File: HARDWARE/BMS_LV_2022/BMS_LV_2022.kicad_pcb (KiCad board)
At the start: 2 copper layers, 90 x 45 mm, 169 parts, among them J1 Conn_01x06_Male, J10 Conn_01x01_Female, J2 Conn_01x12_Male, J3 USB_B_Mini, J4 Conn_01x01_Female, J5 Conn_01x01_Female, J6 Conn_01x01_Female, J7 Conn_01x01_Female, J8 Conn_01x01_Female, J9 Conn_01x01_Female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

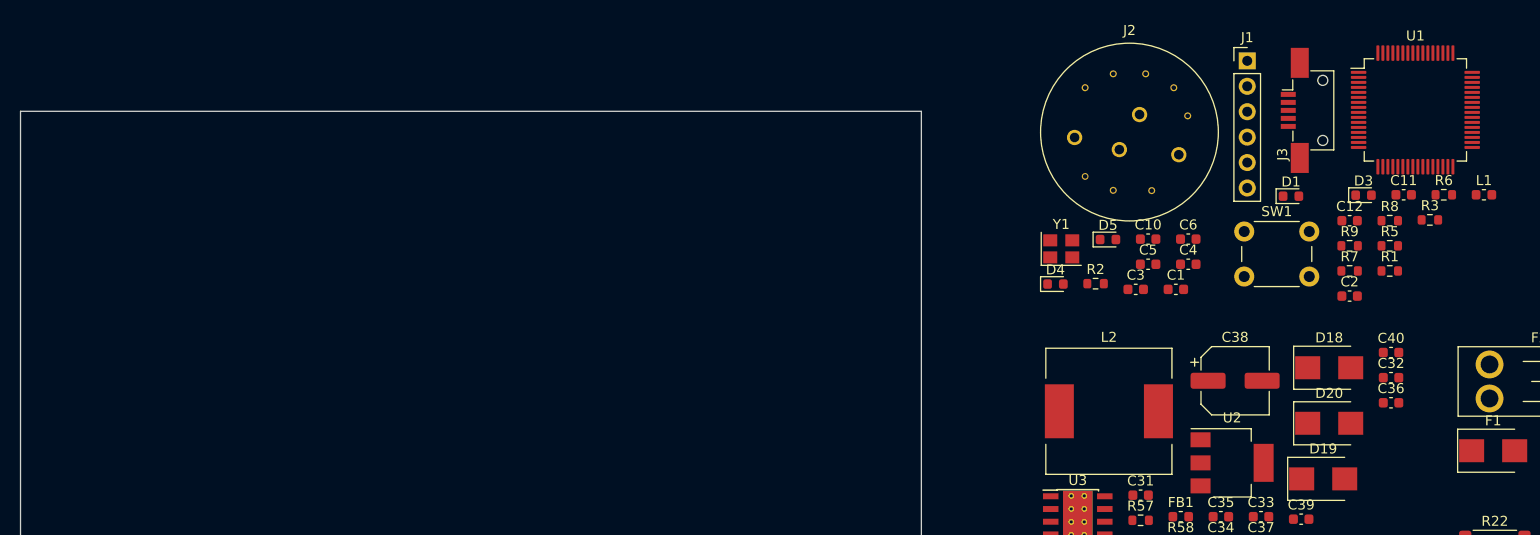
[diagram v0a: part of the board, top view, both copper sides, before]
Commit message: Thermistors change
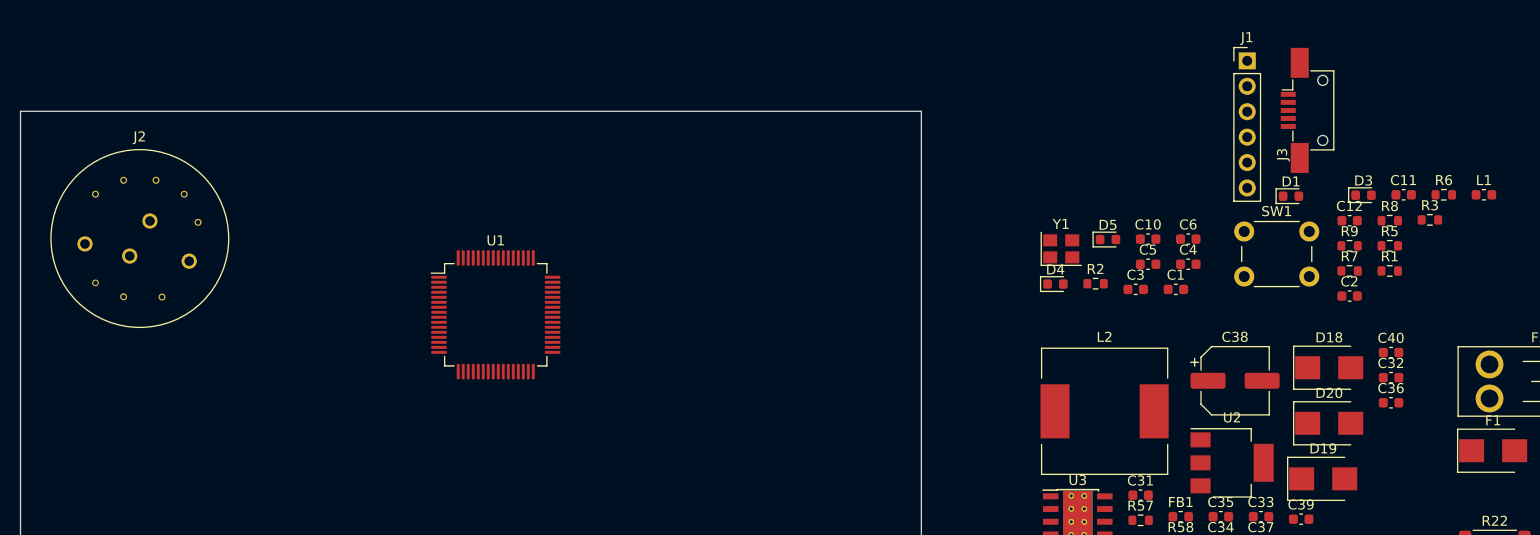
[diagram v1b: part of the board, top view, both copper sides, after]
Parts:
- moved J2 99.4 mm to (121.9, 92.7)
- moved U1 94.1 mm to (157.5, 100.3)
- moved L2 0.43 mm to (218.3, 110.0)

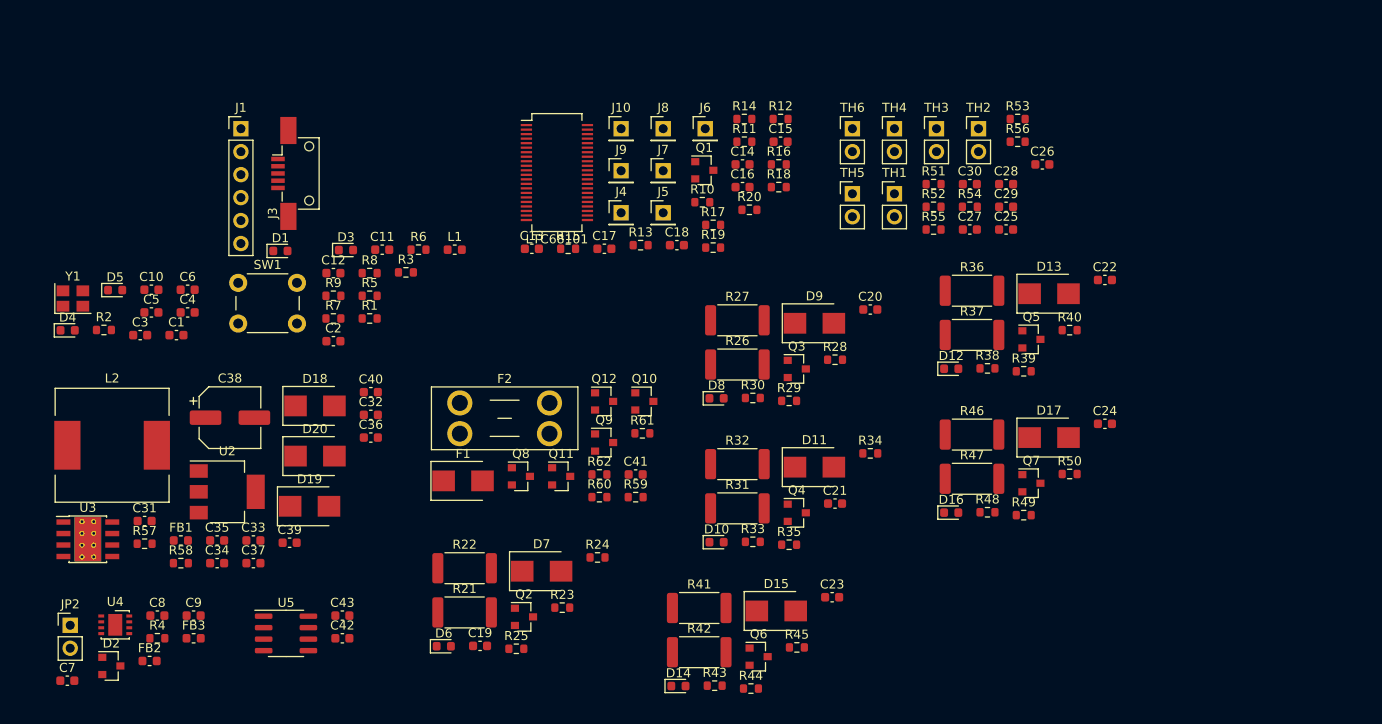
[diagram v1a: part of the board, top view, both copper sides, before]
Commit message: PCB update
Parts changed due to smaller footprints
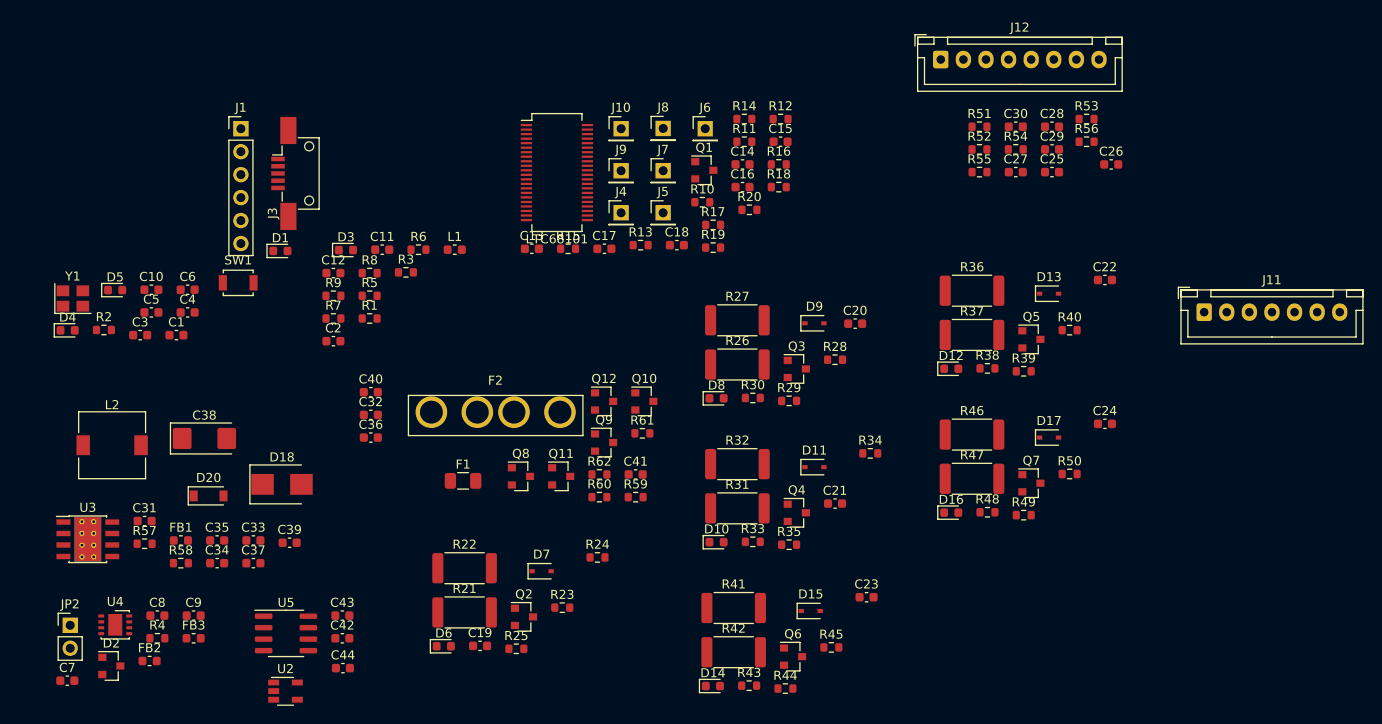
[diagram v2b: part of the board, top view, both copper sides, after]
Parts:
- removed D19: D_Schottky, Diode_SMD:D_SMB
- removed TH1, TH2, TH3, TH4, TH5, TH6: Thermistor_PTC, Connector_PinHeader_2.54mm:PinHeader_1x02_P2.54mm_Vertical
- added C44: 100nF, Capacitor_SMD:C_0603_1608Metric, F.Cu at (243.8, 134.6)
- added J11: Conn_01x07_Female, Connector_JST:JST_XH_B7B-XH-A_1x07_P2.50mm_Vertical, F.Cu at (339.1, 95.2)
- added J12: Conn_01x08_Female, Connector_JST:JST_XH_B8B-XH-A_1x08_P2.50mm_Vertical, F.Cu at (310.0, 67.3)
- C34, C36: value 100nF -> 1uF
- C38: footprint Capacitor_SMD:CP_Elec_6.3x7.7 -> Capacitor_Tantalum_SMD:CP_EIA-6032-28_Kemet-C
- D11, D13, D15, D17, D7, D9: footprint Diode_SMD:D_SMB -> Diode_SMD:D_SOD-323
- D20: footprint Diode_SMD:D_SMB -> Diode_SMD:D_SOD-123
- F1: footprint Diode_SMD:D_SMB -> Fuse:Fuse_1206_3216Metric
- F2: footprint Fuse:Fuseholder_Blade_Mini_Keystone_3568 -> footprints:Fuseholder_Keystone_3522-2
- L2: footprint Inductor_SMD:L_12x12mm_H8mm -> Inductor_SMD:L_7.3x7.3_H4.5
- R4: value 120R -> 120
- SW1: footprint Button_Switch_THT:SW_PUSH_6mm -> Button_Switch_SMD:SW_SPST_B3U-1000P
- U2: value LM1117-3.3 -> LD3985M33R_TSOT23; footprint Package_TO_SOT_SMD:SOT-223-3_TabPin2 -> Package_TO_SOT_SMD:TSOT-23-5
- moved U2 23.0 mm to (237.5, 137.2)
- moved D20 12.6 mm to (229.0, 115.6)
- moved D18 9.41 mm to (237.1, 114.3)
- moved C28 8.13 mm to (322.3, 74.7)
- moved C30 8.13 mm to (318.3, 74.7)
- moved R51 8.13 mm to (314.2, 74.7)
- moved C25 8.13 mm to (322.3, 79.8)
- moved C27 8.13 mm to (318.3, 79.8)
- moved C29 8.13 mm to (322.3, 77.2)
- moved R52 8.13 mm to (314.2, 77.2)
- moved R54 8.13 mm to (318.3, 77.2)
- moved R55 8.13 mm to (314.2, 79.8)
- moved C26 7.62 mm to (328.8, 78.9)
- moved R53 7.62 mm to (326.1, 73.9)
- moved R56 7.62 mm to (326.1, 76.4)
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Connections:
- net /LTC6810/Balance1/Cell renamed /LTC6810/CellBalance2
- net /LTC6810/Balance2/Cell renamed /LTC6810/CellBalance3
- net /LTC6810/Balance3/Cell renamed /LTC6810/CellBalance4
- net /LTC6810/Balance4/Cell renamed /LTC6810/CellBalance5
- net /LTC6810/Balance5/Cell renamed /LTC6810/CellBalance6
- J2 pad 10: Net-(J2-Pad10) -> /V_Out
- J2 pad 11: /V_Out -> GND
- J2 pad 9: Net-(J2-Pad9) -> /V_Out
- U2 pad 1: GND -> +5VD
- U2 pad 2: +3V3 -> GND
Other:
- copper layers 2 -> 4

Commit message: PCB Layout Update
Some work on PCB Layout
+ AS214-97PN (connector) 3D model added
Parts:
- removed J10, J4, J5, J6, J7, J8, J9: Conn_01x01_Female, Connector_PinHeader_2.54mm:PinHeader_1x01_P2.54mm_Vertical
- moved C24 217.1 mm to (111.7, 89.5), turned to 270 degrees
- moved R50 212.3 mm to (113.2, 89.5), turned to 270 degrees
- moved D17 207.9 mm to (114.9, 89.6), turned to 270 degrees
- moved R49 204.5 mm to (116.6, 89.5), turned to 270 degrees
- moved Q7 202.4 mm to (119.0, 89.8)
- moved R46 201.5 mm to (113.5, 84.2), turned to 90 degrees
- moved R48 198.3 mm to (120.0, 81.9), turned to 90 degrees
- moved R47 198.3 mm to (117.3, 84.2), turned to 90 degrees
- moved D16 193.6 mm to (120.0, 86.5), turned to 90 degrees
- moved C22 184.4 mm to (143.7, 93.7), turned to 180 degrees
- moved D13 182.2 mm to (139.8, 89.6), turned to 270 degrees
- moved R40 180.6 mm to (143.7, 92.2), turned to 180 degrees
- moved R39 178.1 mm to (141.5, 89.5), turned to 270 degrees
- moved Q5 176.3 mm to (143.9, 89.8)
- moved R36 175.3 mm to (138.4, 84.2), turned to 90 degrees
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
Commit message: PCB Layout Update 2
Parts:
- moved C9 98.4 mm to (132.1, 103.8), turned to 90 degrees
- moved FB3 97.2 mm to (134.9, 101.4)
- moved D1 95.2 mm to (178.4, 120.2), turned to 270 degrees
- moved FB2 94.3 mm to (132.1, 106.7), turned to 270 degrees
- moved SW1 94.1 mm to (145.7, 113.1), turned to 180 degrees
- moved R4 93.7 mm to (132.1, 109.7), turned to 90 degrees
- moved D3 93.5 mm to (179.9, 120.2), turned to 270 degrees
- moved D2 93.1 mm to (132.6, 97.6), turned to 195 degrees
- moved R2 93.1 mm to (178.4, 123.2), turned to 270 degrees
- moved D4 91.8 mm to (181.4, 120.2), turned to 270 degrees
- moved C8 91.7 mm to (134.9, 104.4)
- moved R3 91.3 mm to (179.9, 123.2), turned to 270 degrees
- moved C1 90.6 mm to (148.9, 113.3), turned to 90 degrees
- moved D5 90.1 mm to (182.8, 120.2), turned to 270 degrees
- moved R5 89.5 mm to (181.4, 123.2), turned to 270 degrees
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
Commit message: PCB Layout Update 3
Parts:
- removed R13, R14, R15: 10k, Resistor_SMD:R_0603_1608Metric
- added J4: Battery+, footprints:CellPad, F.Cu at (114.1, 91.7)
- added J5: Battery-, footprints:CellPad, F.Cu at (114.1, 115.3)
- Q11, Q12, Q8, Q9: value Q_PMOS_GSD -> SiSS05DN; footprint Package_TO_SOT_SMD:SOT-23 -> Package_SO:Vishay_PowerPAK_1212-8_Single
- moved Q9 117.2 mm to (116.4, 85.9), turned to 180 degrees
- moved Q10 116.1 mm to (129.1, 82.1)
- moved R61 116.1 mm to (126.7, 82.0)
- moved R59 116.1 mm to (132.3, 83.1), turned to 0 degrees
- moved R60 116.0 mm to (132.3, 81.7), turned to 0 degrees
- moved Q12 114.4 mm to (120.8, 82.3), turned to 0 degrees
- moved Q8 114.3 mm to (116.4, 82.3), turned to 180 degrees
- moved C41 114.2 mm to (124.4, 82.7)
- moved R62 114.0 mm to (124.4, 81.2)
- moved Q11 110.3 mm to (120.7, 85.9), turned to 0 degrees
- moved F1 108.8 mm to (120.6, 92.6), turned to 90 degrees
- moved F2 96.7 mm to (132.8, 86.2), turned to 180 degrees
- moved C42 84.1 mm to (141.6, 93.0)
- moved U5 84.1 mm to (137.2, 91.6)
- moved C43 83.0 mm to (142.4, 89.7), turned to 0 degrees
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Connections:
- C13 pad 2: GND -> GNDPWR
- C14 pad 2: GND -> GNDPWR
- C15 pad 2: GND -> GNDPWR
- C16 pad 2: GND -> GNDPWR
- C17 pad 2: GND -> GNDPWR
- C18 pad 1: GND -> GNDPWR
- C19 pad 2: GND -> GNDPWR
- C20 pad 2: GND -> GNDPWR
- C21 pad 2: GND -> GNDPWR
- C22 pad 2: GND -> GNDPWR
- C23 pad 2: GND -> GNDPWR
- C24 pad 2: GND -> GNDPWR
- D17 pad 2: GND -> GNDPWR
- J11 pad 1: +24V -> +BATT
- J11 pad 7: GND -> GNDPWR
- J2 pad 6: Net-(J2-Pad6) -> VCC
- J2 pad 8: VCC -> Net-(J2-Pad8)
- LTC68101 pad 1: GND -> GNDPWR
- LTC68101 pad 21: GND -> GNDPWR
- LTC68101 pad 22: GND -> GNDPWR
- LTC68101 pad 23: GND -> GNDPWR
- LTC68101 pad 24: GND -> GNDPWR
- LTC68101 pad 28: GND -> GNDPWR
- LTC68101 pad 29: GND -> GNDPWR
- LTC68101 pad 35: Net-(LTC68101-Pad35) -> Net-(LTC68101-Pad34)
- LTC68101 pad 38: Net-(LTC68101-Pad38) -> Net-(LTC68101-Pad34)
- LTC68101 pad 39: Net-(LTC68101-Pad39) -> Net-(LTC68101-Pad34)
- LTC68101 pad 43: GND -> GNDPWR
- LTC68101 pad 44: GND -> GNDPWR
- Q11 pad 1: /eFuse/Gate -> Net-(C41-Pad2)
- Q11 pad 3: Net-(F2-Pad2) -> Net-(C41-Pad2)
- Q12 pad 1: /eFuse/Gate -> Net-(C41-Pad2)
- Q12 pad 3: Net-(F2-Pad2) -> Net-(C41-Pad2)
- Q7 pad 2: GND -> GNDPWR
- Q8 pad 1: /eFuse/Gate -> Net-(C41-Pad2)
- Q8 pad 3: +24V -> Net-(C41-Pad2)
- Q9 pad 1: /eFuse/Gate -> Net-(C41-Pad2)
- Q9 pad 3: +24V -> Net-(C41-Pad2)
- R10 pad 2: +24V -> +BATT
- R11 pad 2: +24V -> +BATT
- R12 pad 1: GND -> GNDPWR
- R12 pad 2: Net-(LTC68101-Pad39) -> Net-(LTC68101-Pad34)
- R19 pad 2: +24V -> +BATT
- R21 pad 2: +24V -> +BATT
- R22 pad 2: +24V -> +BATT
- R23 pad 2: +24V -> +BATT
- R49 pad 2: GND -> GNDPWR
- R50 pad 2: GND -> GNDPWR
- Y1 pad 1: Net-(C5-Pad2) -> Net-(C6-Pad2)
- Y1 pad 2: Net-(C6-Pad2) -> GND
- Y1 pad 3: (no net) -> Net-(C5-Pad2)
- Y1 pad 4: (no net) -> GND
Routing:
- net /LTC6810/CellBalance5: track 0.00 -> 34.6 mm
- net /LTC6810/CellBalance3: track 0.00 -> 34.0 mm
- net /LTC6810/CellBalance4: track 0.00 -> 25.0 mm
- net /LTC6810/CellBalance2: track 0.00 -> 23.2 mm
- net /LTC6810/CellBalance6: track 0.00 -> 20.5 mm
- net +BATT: track 0.00 -> 16.0 mm
- net GNDPWR: track 0.00 -> 11.8 mm
- net /VCC_Pin: track 0.00 -> 3.43 mm
- net (no net): vias 0 -> 4

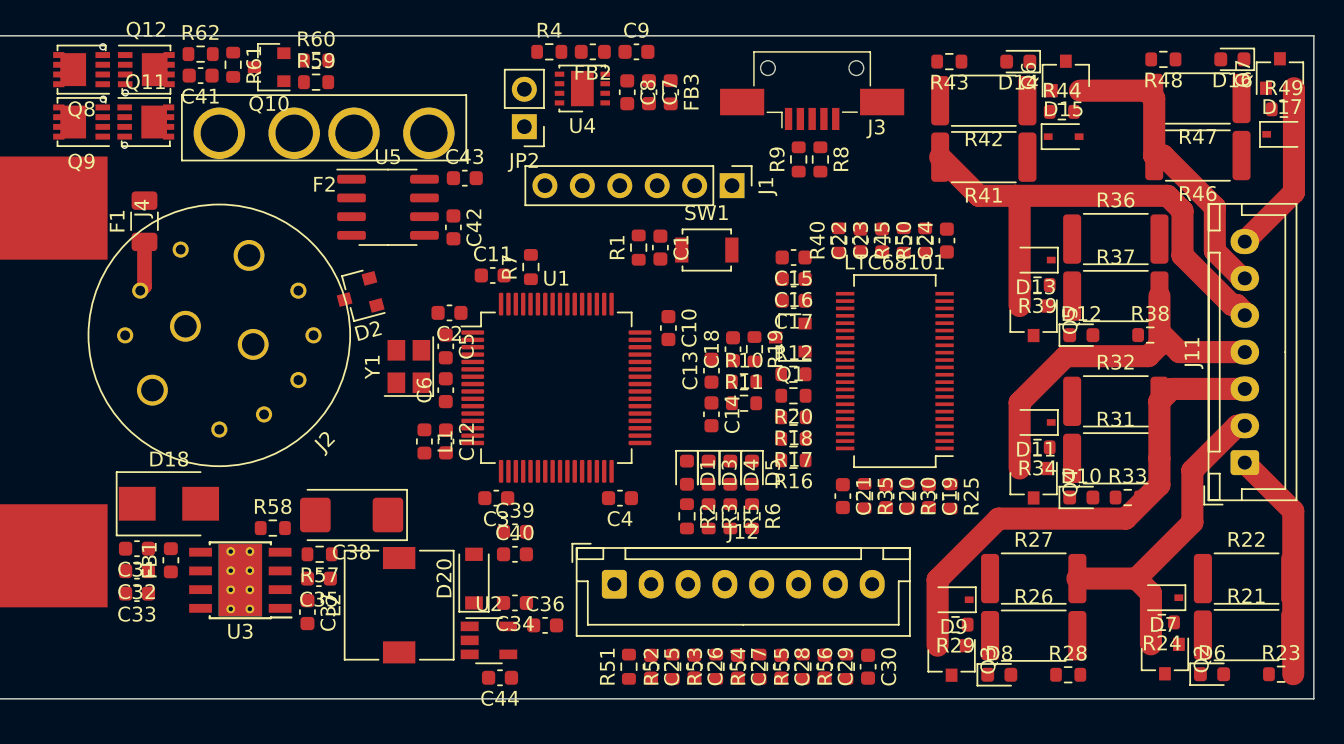
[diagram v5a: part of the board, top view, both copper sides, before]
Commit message: Power planes added
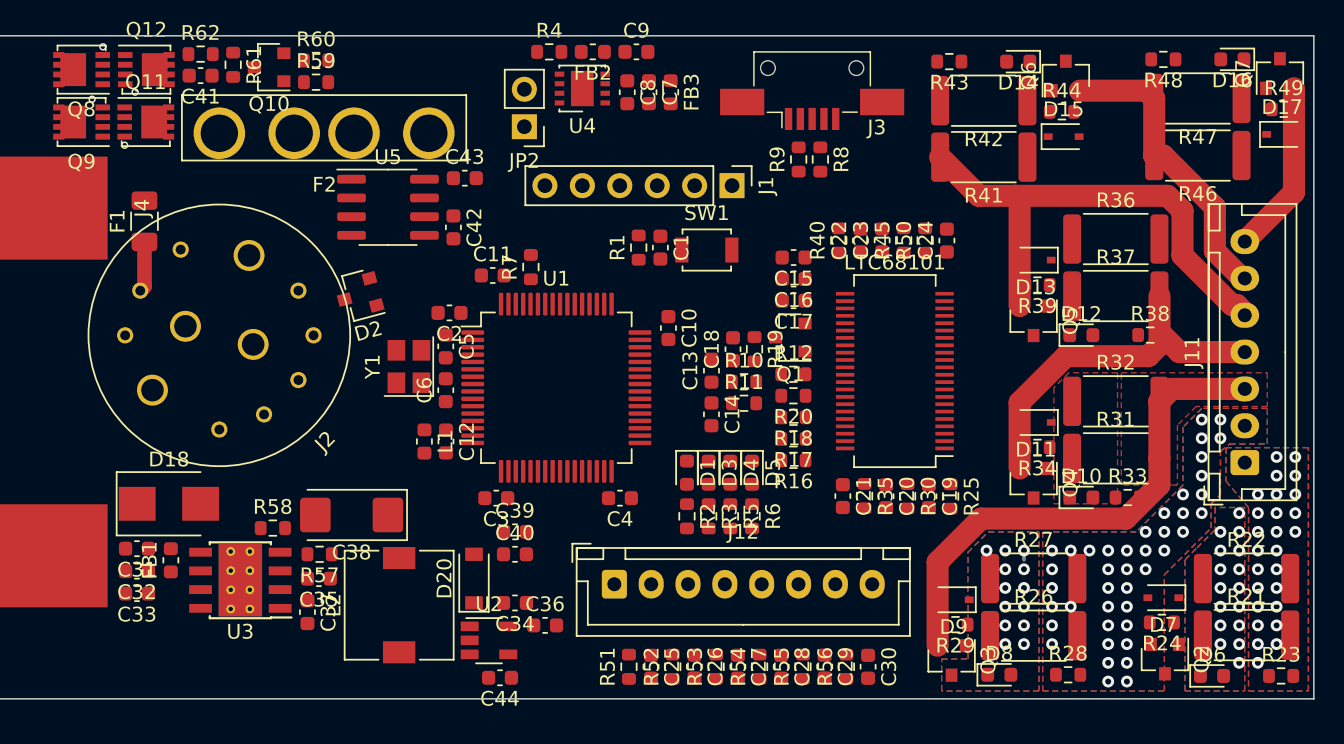
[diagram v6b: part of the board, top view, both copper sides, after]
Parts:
- moved D6 0.11 mm to (193.1, 123.4)
- moved R23 0.11 mm to (197.8, 123.4)
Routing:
- net /LTC6810/CellBalance2: track 23.2 -> 0.64 mm, vias 0 -> 42
- net +BATT: track 16.0 -> 0.29 mm, vias 0 -> 26
- net /LTC6810/CellBalance3: track 34.0 -> 34.7 mm
- net Net-(D8-Pad1): track 0.00 -> 0.63 mm, vias 0 -> 13
- net Net-(D6-Pad1): vias 0 -> 16
- added copper zone on B.Cu, net +BATT
- added copper zone on F.Cu, net +BATT
- added copper zone on B.Cu, net /LTC6810/CellBalance2
- added copper zone on F.Cu, net /LTC6810/CellBalance2
- added copper zone on F.Cu, net /LTC6810/CellBalance3
- added copper zone on In2.Cu, net GND
- added copper zone on In2.Cu, net GNDPWR
- added copper zone on F.Cu, net Net-(D10-Pad1)
- added copper zone on B.Cu, net Net-(D6-Pad1)
- added copper zone on F.Cu, net Net-(D6-Pad1)
- added copper zone on B.Cu, net Net-(D8-Pad1)
- added copper zone on F.Cu, net Net-(D8-Pad1)
